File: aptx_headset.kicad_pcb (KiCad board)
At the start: 2 copper layers, 65.4 x 32.3 mm, 63 parts, among them J1 AudioJack4, J2 Conn_01x03, SW1 vol+, SW2 vol-, SW3 next, SW4 prev, SW5 pp/call, SW6 mute, U1 OPA1664, U2 CSR8645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

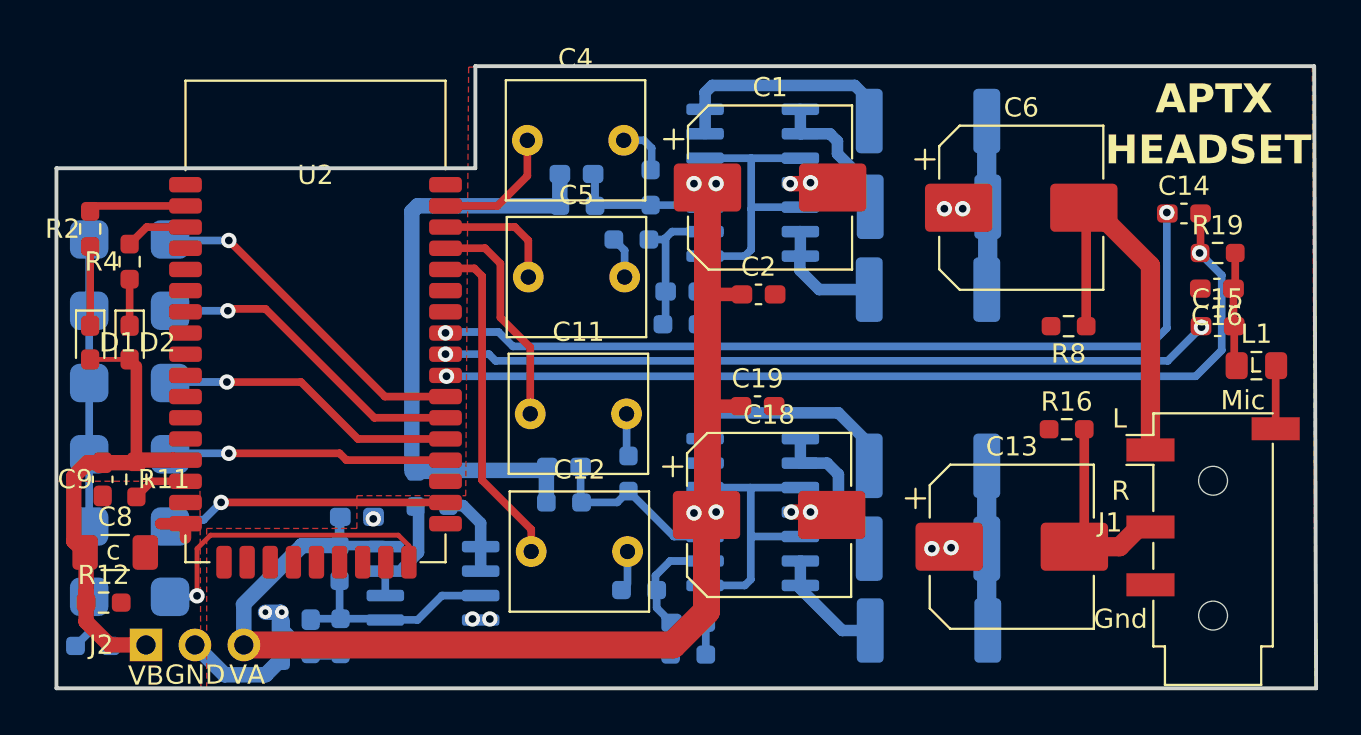
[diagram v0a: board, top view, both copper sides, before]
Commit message: separate buffered VGND
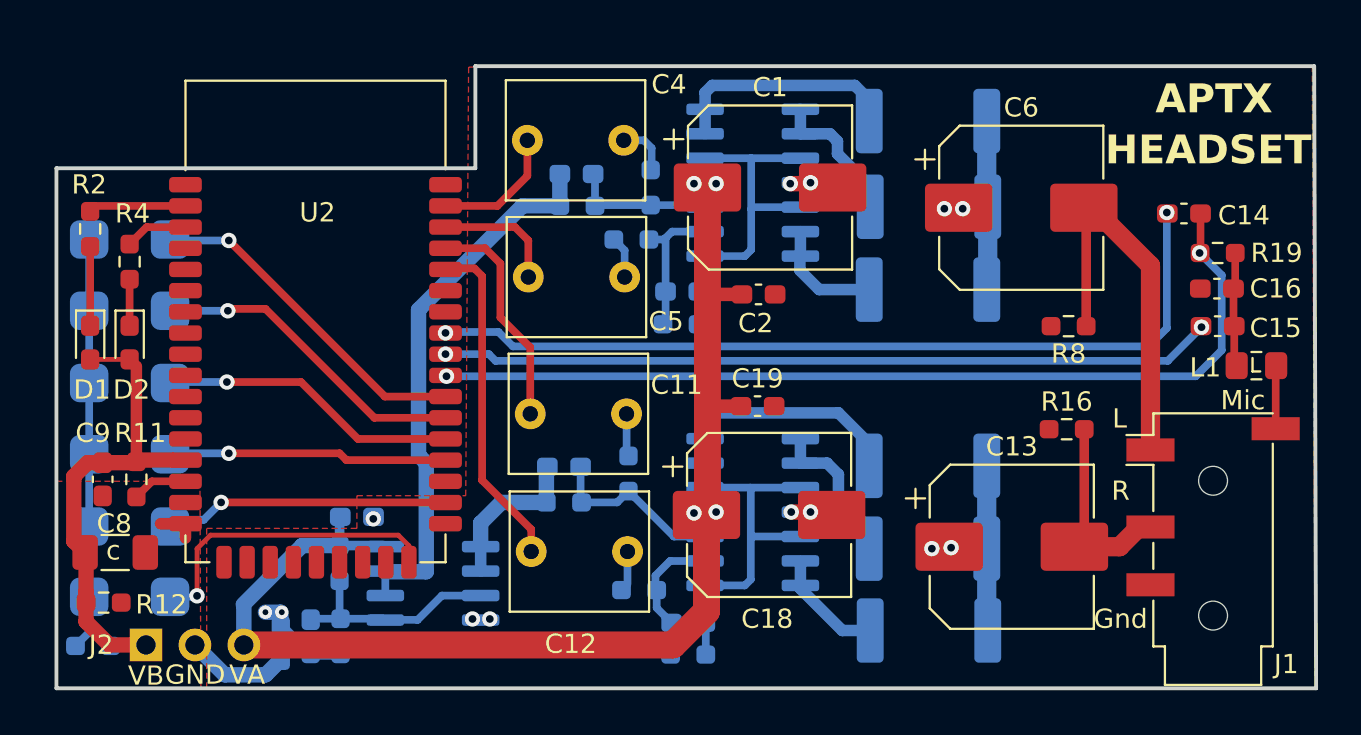
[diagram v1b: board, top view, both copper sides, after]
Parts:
- removed R25, R28: 0R5, 00_hari:R_0603_1608Metric_Pad0.98x0.95mm_HandSolder
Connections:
- C10 pad 1: /VGND -> /VGND_R
- C3 pad 1: /VGND -> /VGND_L
- R1 pad 1: /VGND -> /VGND_L
- R13 pad 1: /VGND -> /VGND_R
- U4 pad 1: Net-(U4A--) -> /VGND_R
- U4 pad 2: Net-(U4A--) -> /VGND_R
- U4 pad 6: Net-(U4B--) -> /VGND_L
- U4 pad 7: Net-(U4B--) -> /VGND_L
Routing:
- net /VGND: track 32.0 -> 0.00 mm
- net /VGND_L: track 0.00 -> 28.3 mm
- net /VGND_R: track 0.00 -> 8.15 mm
- net Net-(U4B--): track 4.46 -> 0.00 mm
- net Net-(U4A--): track 4.39 -> 0.00 mm

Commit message: move buttons
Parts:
- moved SW1 1.56 mm to (89.5, 76.3)
- moved SW2 1.25 mm to (89.5, 80.3)
- moved SW3 1.06 mm to (89.5, 84.2)
- moved SW4 0.86 mm to (89.5, 88.2)
- moved SW5 0.63 mm to (89.5, 92.2)
- moved SW6 0.40 mm to (89.5, 96.0)
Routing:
- net Net-(R21-Pad2): track 21.4 -> 22.9 mm
- net /VOL+: track 17.7 -> 18.5 mm
- net /VGND_L: track 28.3 -> 27.6 mm
- net /VOL-: track 16.7 -> 17.3 mm
- net /NEXT: track 15.5 -> 16.1 mm
